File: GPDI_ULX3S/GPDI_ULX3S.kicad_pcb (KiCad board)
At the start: 4 copper layers, 40 x 23 mm, 51 parts, among them J2 CONN, U1 RN5RK501A, U2 PCA9306

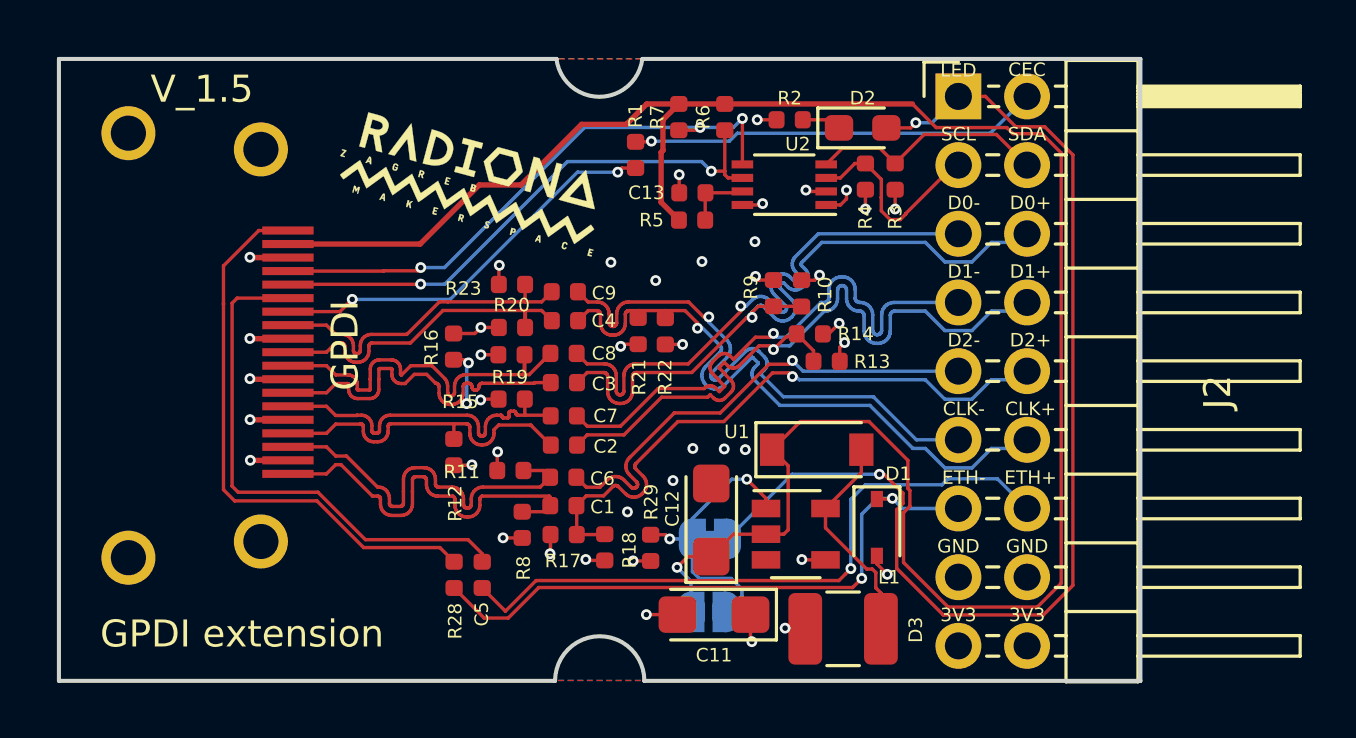
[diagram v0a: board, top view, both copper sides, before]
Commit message: GPDI update to KiCad 7, update PCA9306 package, Version to v1.6
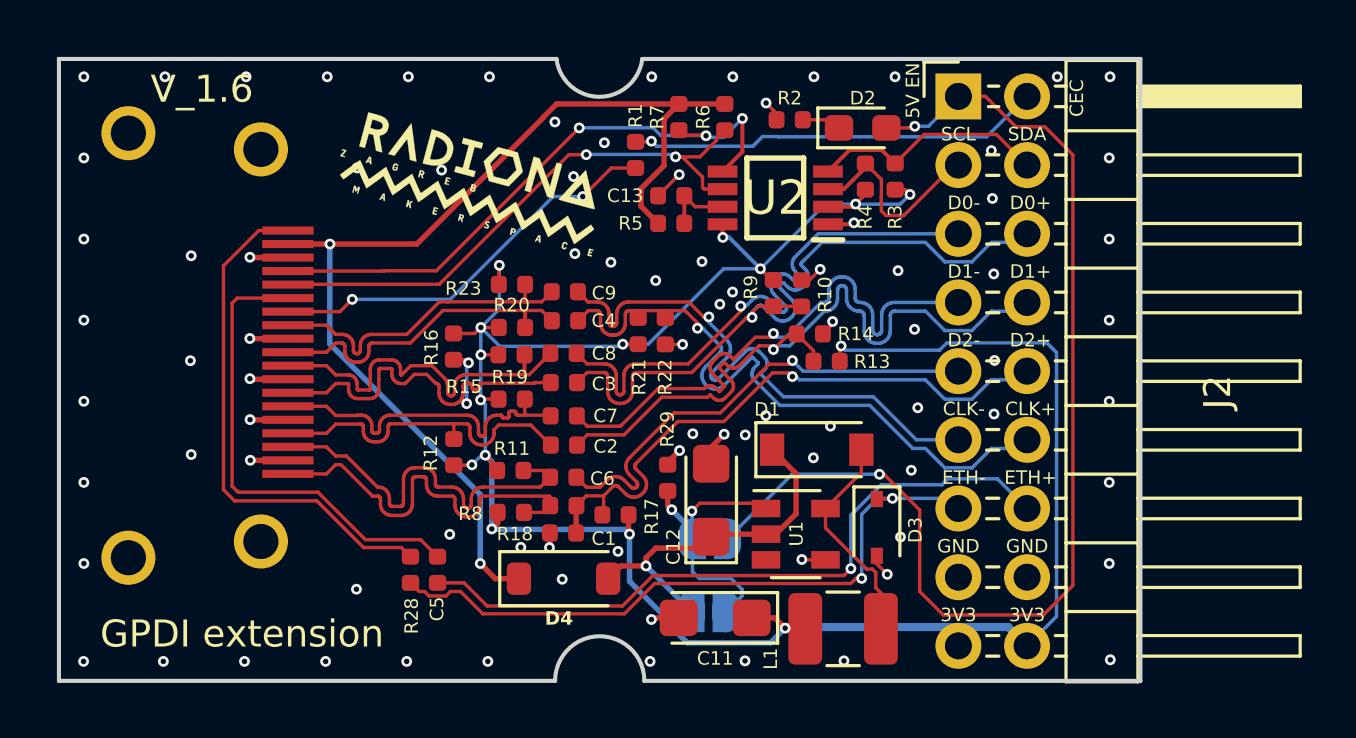
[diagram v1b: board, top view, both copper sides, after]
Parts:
- added D4: MBR0520, Diode_SMD:D_SOD-123, F.Cu at (129.2, 85.1)
- added G***: LOGO, intergalaktik:intergalaktik, B.Cu at (123.7, 86.0)
- U2: footprint Package_SO:VSSOP-8_2.3x2mm_P0.5mm -> PCA9306:SOP65P400X130-8N
- moved R29 2.67 mm to (133.0, 81.4), turned to 90 degrees
- moved R17 2.05 mm to (131.1, 82.8), turned to 180 degrees
- moved C5 1.66 mm to (124.5, 84.8)
- moved R18 1.63 mm to (129.1, 83.5), turned to 180 degrees
- moved R28 1.62 mm to (123.5, 84.8)
- moved C13 0.79 mm to (133.1, 71.0)
- moved R5 0.78 mm to (133.1, 72.0)
- moved C12 0.73 mm to (134.6, 82.2)
- moved R8 0.62 mm to (127.2, 82.7), turned to 0 degrees
- moved U2 0.59 mm to (137.0, 71.1)
- moved C11 0.13 mm to (134.8, 86.6)
- renumbered GPDI to P1
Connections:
- C12 pad 1: +5V -> Net-(D1-K)
- D1 pad 1: +5V -> Net-(D1-K)
- D2 pad 2: LED_HDMI -> 5V_ENABLE
- J2 pad 1: LED_HDMI -> 5V_ENABLE
- JP1 pad 1: LED_HDMI -> 5V_ENABLE
- JP1 pad 2: Net-(JP1-Pad2) -> 5V_ENABLE
- JP2 pad 1: +5V -> Net-(D1-K)
- JP2 pad 2: Net-(JP1-Pad2) -> 5V_ENABLE
- R29 pad 1: Net-(JP1-Pad2) -> 5V_ENABLE
- U1 pad 1: Net-(JP1-Pad2) -> 5V_ENABLE
- U1 pad 2: +5V -> Net-(D1-K)
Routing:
- net +3V3: track 13.5 -> 87.4 mm, vias 17 -> 15
- net 5V_ENABLE: track 0.00 -> 54.8 mm, vias 0 -> 4
- net +5V: track 87.5 -> 39.3 mm, vias 1 -> 2
- net LED_HDMI: track 43.2 -> 0.00 mm, vias 2 -> 0
- net Net-(D1-K): track 0.00 -> 13.2 mm, vias 0 -> 1
- net Net-(JP1-Pad2): track 10.7 -> 0.00 mm, vias 2 -> 0
- net GND: track 19.9 -> 17.5 mm, vias 25 -> 85
- net /ETH+: track 19.5 -> 17.6 mm
- net GPDI_ETH-: track 23.1 -> 24.8 mm
- net /ETH-: track 20.9 -> 19.2 mm
- net GPDI_ETH+: track 24.5 -> 25.7 mm
- net GPDI_SDA: track 21.7 -> 22.8 mm
- net GPDI_SCL: track 20.5 -> 21.1 mm
- added copper zone on In1.Cu, net GND
- added copper zone on In2.Cu, net GND
- removed copper zone on VCC.Cu, net +3V3
- removed copper zone on B.Cu, net GND
- removed copper zone on F.Cu, net GND
- removed copper zone on GND.Cu, net GND
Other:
- outline, holes or cut-outs redrawn
- net class Default removed
- board text added: "5V EN"
- board text added: "V_1.6"
- board text removed: "LED"
- board text removed: "V_1.5"
